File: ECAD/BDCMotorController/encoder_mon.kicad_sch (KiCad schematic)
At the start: 12 parts, among them U70 74AHC00, U71 74AHC00, U72 74AHC1G17, U73 74AHC1G17, U74 74AHC00

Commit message: Progressed ECAD.
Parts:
- renumbered C145 to C144, C146 to C145, C147 to C146, C148 to C147, C149 to C148, U70 to U69, U71 to U70, U72 to U71, U73 to U72, U74 to U73

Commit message: Progressed ECAD.
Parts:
- C144, C145, C148: Status OK -> (none)
- R68, R69: MPN AC0805FR-7W1KL -> (none)
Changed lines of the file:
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@@
 			)
 		)
-		(property "Status" "OK"
+		(property "Status" ""
 			(at 135.89 173.99 0)
 			(effects
@@
 			)
 		)
-		(property "Status" "OK"
+		(property "Status" ""
 			(at 83.82 172.72 0)
 			(effects
@@
 			)
 		)
-		(property "Datasheet" "https://datasheet.lcsc.com/lcsc/2010202005_YAGEO-AC0805FR-7W1KL_C727989.pdf"
+		(property "Datasheet" ""
 			(at 92.71 111.76 0)
 			(effects
@@
 			)
 		)
-		(property "MPN" "AC0805FR-7W1KL"
+		(property "MPN" ""
 			(at 92.71 111.76 90)
 			(effects
@@
 			)
 		)
-		(property "Datasheet" "https://datasheet.lcsc.com/lcsc/2010202005_YAGEO-AC0805FR-7W1KL_C727989.pdf"
+		(property "Datasheet" ""
 			(at 92.71 68.58 0)
 			(effects
@@
 			)
 		)
-		(property "MPN" "AC0805FR-7W1KL"
+		(property "MPN" ""
 			(at 92.71 68.58 90)
 			(effects
@@
 			)
 		)
-		(property "Status" "OK"
+		(property "Status" ""
 			(at 31.75 175.26 0)
 			(effects

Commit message: Progressed ECAD.
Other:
- note added: "333us min"
- note added: "Input square wave max frequency = 3 kHz (typical hall efect encoder frequency at max motor speed with no load)"
- note added: "t"
- note added: "tmin = 62.5ns @ fMCU = 16MHz"
- moved on the sheet: C146, C147, R68, R69, U69A, U69B, U69C, U69D, U70A, U70B, U70C, U70D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

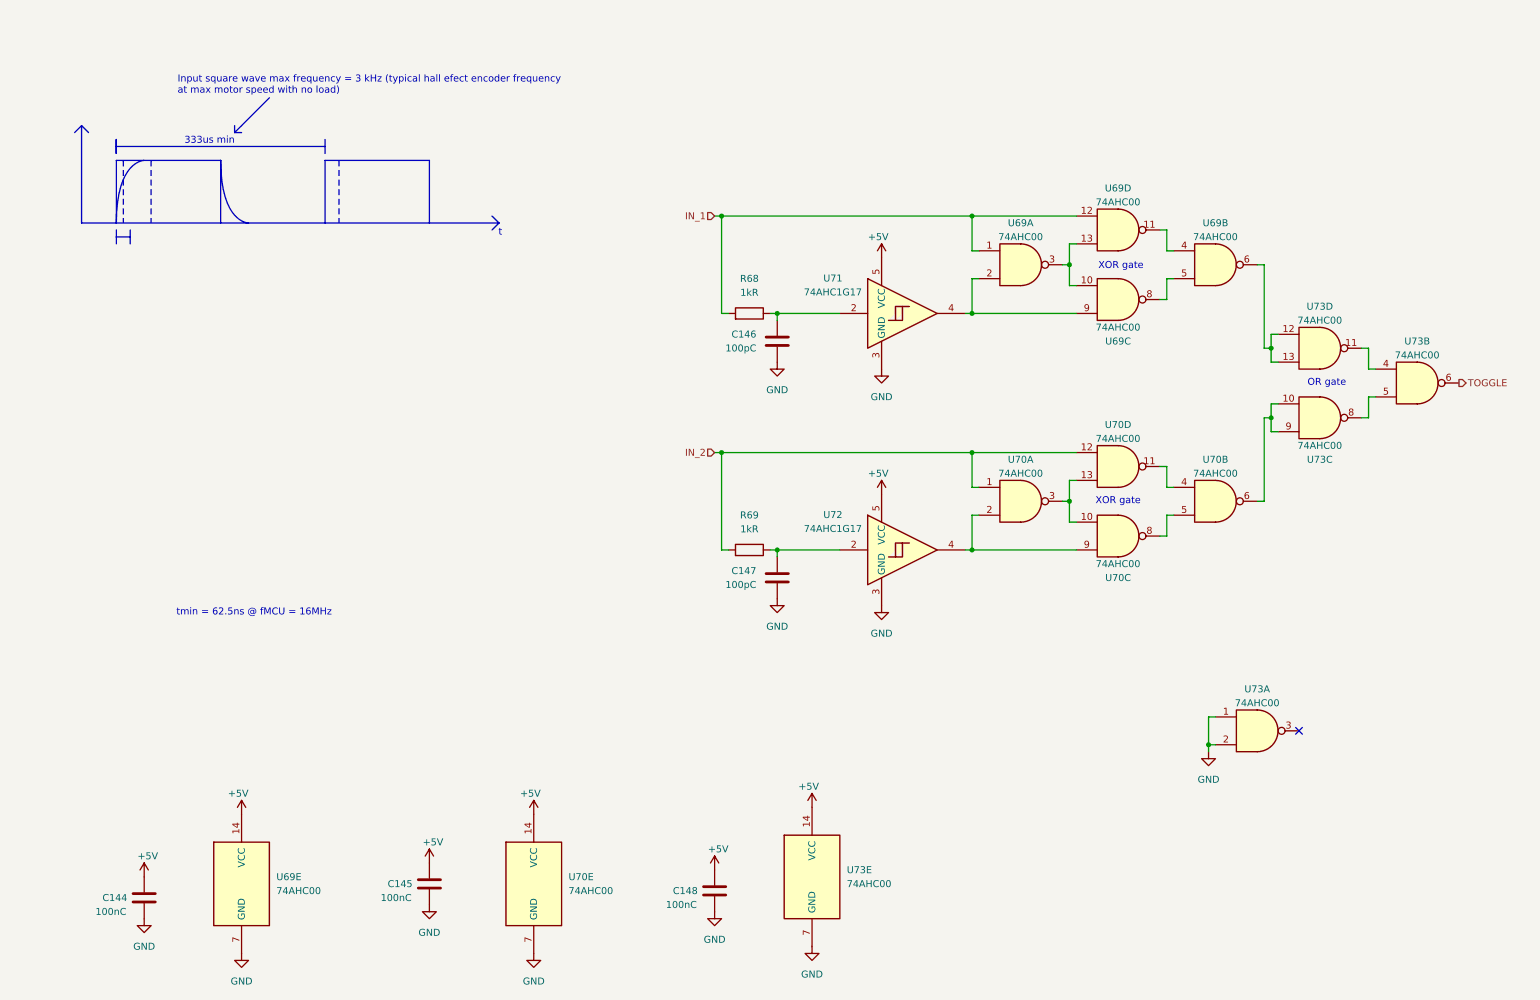
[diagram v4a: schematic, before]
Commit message: Update encoder_mon.kicad_sch
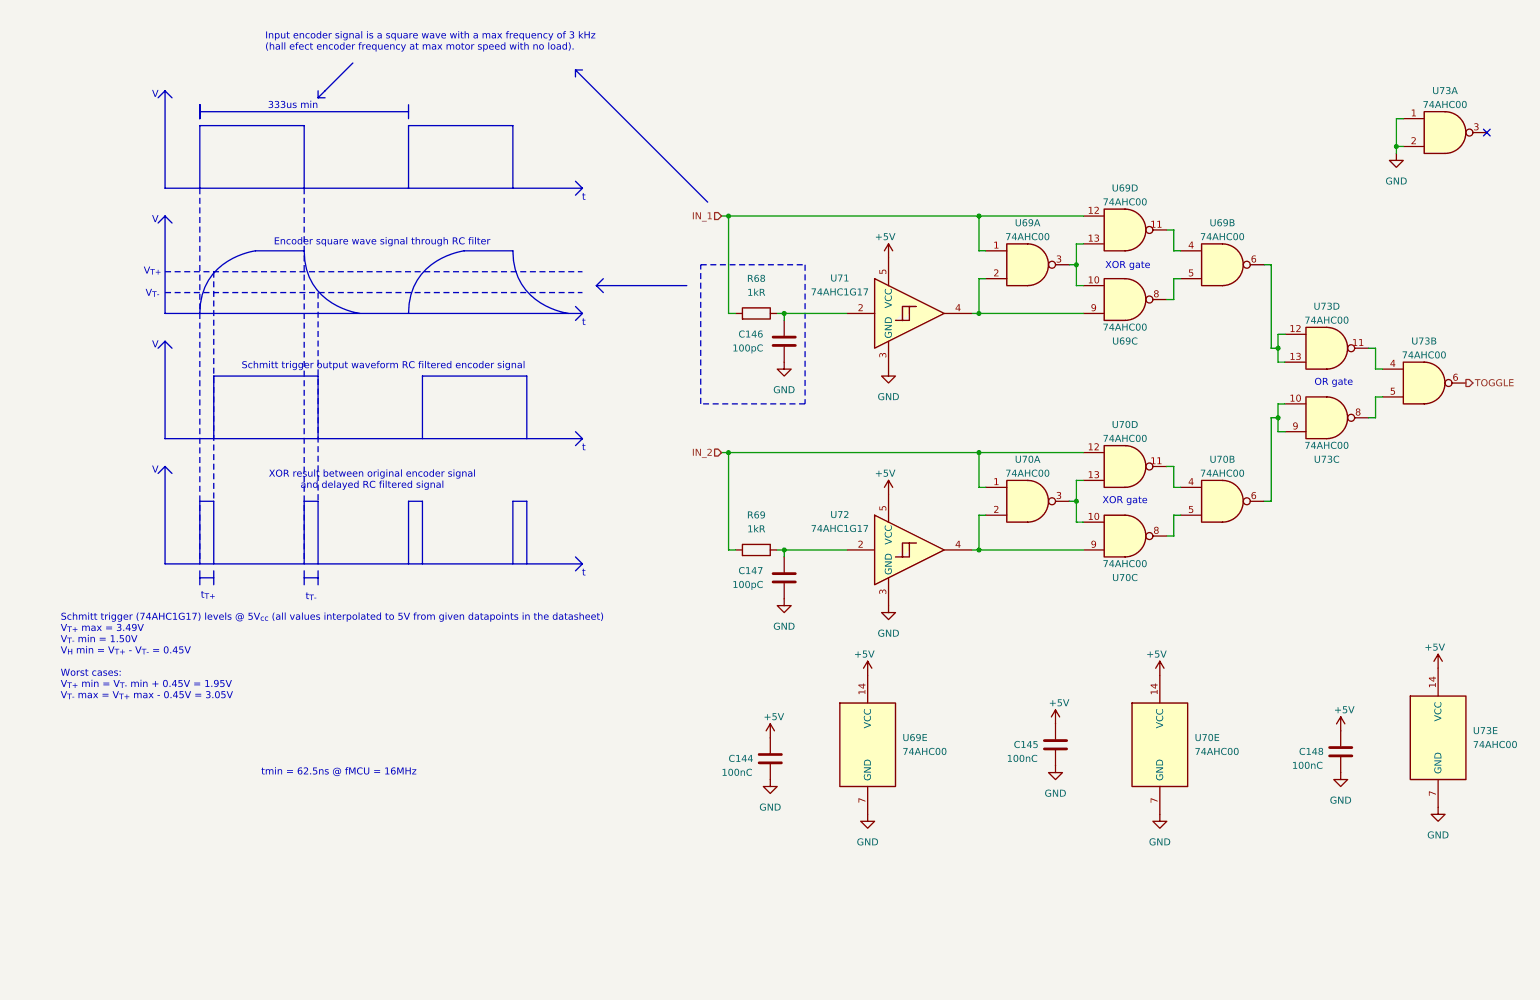
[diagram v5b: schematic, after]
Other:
- note added: "Encoder square wave signal through RC filter"
- note added: "Input encoder signal is a square wave with a max frequency of 3 kHz (hall efect encoder frequency at max motor speed with no load)."
- note added: "Schmitt trigger (74AHC1G17) levels @ 5V_{cc} (all values interpolated to 5V from given datapoints in the datasheet) V_{T+} max = 3.49V V_{T-} min = 1.50V V_{H} min = V_{T+} - V_{T-} = 0.45V Worst cases: V_{T+} min = V_{T-} min + 0.45V = 1.95V V_{T-} max = V_{T+} max - 0.45V = 3.05V"
- note added: "Schmitt trigger output waveform RC filtered encoder signal"
- note added: "V"
- note added: "V_{T+}"
- note added: "V_{T-}"
- note added: "XOR result between original encoder signal and delayed RC filtered signal"
- note added: "t_{T+}"
- note added: "t_{T-}"
- note removed: "Input square wave max frequency = 3 kHz (typical hall efect encoder frequency at max motor speed with no load)"
- moved on the sheet: C144, C145, C146, C147, C148, R68, R69, U69A, U69B, U69C, U69D, U69E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

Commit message: Progressed ECAD.
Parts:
- removed C147: 100pC, Capacitor_SMD:C_0805_2012Metric, symbol Device:C
- added C164: 100nC, Capacitor_SMD:C_0805_2012Metric, symbol Device:C
- C146: value 100pC -> 100nC; MPN CC0805KRX7R9BB101 -> (none); Status OK -> (none)
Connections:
- net GND: now also C164.2
- net at R68.1, U71.2: now also C164.1; no longer C146.1
- net at R69.1, U72.2: now also C146.1
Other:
- note added: "62.5ns < t_{T+} < 333us / 2 62.5ns < RC charging to V_{T+} min and V_{T+} max < 166.5us RC charging time to 99.9% < 166.5us"
- note added: "62.5ns < t_{T+} < 333us / 2 62.5ns < RC discharging to V_{T-} min and V_{T-} max < 166.5us"
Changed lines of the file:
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@@
 		)
 	)
+	(text "62.5ns < t_{T+} < 333us / 2\n62.5ns < RC discharging to V_{T-} min and V_{T-} max < 166.5us"
+		(exclude_from_sim no)
+		(at 46.736 176.784 0)
+		(effects
+			(font
+				(size 1.27 1.27)
+			)
+		)
+	)
 	(text "V"
 		(exclude_from_sim no)
@@
 		)
 	)
+	(text "62.5ns < t_{T+} < 333us / 2\n62.5ns < RC charging to V_{T+} min and V_{T+} max < 166.5us\n\nRC charging time to 99.9% < 166.5us"
+		(exclude_from_sim no)
+		(at 44.704 160.528 0)
+		(effects
+			(font
+				(size 1.27 1.27)
+			)
+		)
+	)
 	(text "V"
 		(exclude_from_sim no)
@@
 	)
 	(symbol
+		(lib_id "Device:C")
+		(at 148.59 73.66 0)
+		(unit 1)
+		(exclude_from_sim no)
+		(in_bom yes)
+		(on_board yes)
+		(dnp no)
+		(property "Reference" "C164"
+			(at 140.97 73.66 0)
+			(effects
+				(font
+					(size 1.27 1.27)
+				)
+				(justify left)
+			)
+		)
+		(property "Value" "100nC"
+			(at 139.7 76.2 0)
+			(effects
+				(font
+					(size 1.27 1.27)
+				)
+				(justify left)
+			)
+		)
+		(property "Footprint" "Capacitor_SMD:C_0805_2012Metric"
+			(at 149.5552 77.47 0)
+			(effects
+				(font
+					(size 1.27 1.27)
+				)
+				(hide yes)
+			)
+		)
+		(property "Datasheet" ""
+			(at 148.59 73.66 0)
+			(effects
+				(font
+					(size 1.27 1.27)
+				)
+				(hide yes)
+			)
+		)
+		(property "Description" ""
+			(at 148.59 73.66 0)
+			(effects
+				(font
+					(size 1.27 1.27)
+				)
+			)
+		)
+		(property "MPN" ""
+			(at 148.59 73.66 0)
+			(effects
+				(font
+					(size 1.27 1.27)
+				)
+				(hide yes)
+			)
+		)
+		(property "Status" ""
+			(at 148.59 73.66 0)
+			(effects
+				(font
+					(size 1.27 1.27)
+				)
+				(hide yes)
+			)
+		)
+		(property "Sim.Device" ""
+			(at 148.59 73.66 0)
+			(effects
+				(font
+					(size 1.27 1.27)
+				)
+				(hide yes)
+			)
+		)
+		(property "Sim.Pins" ""
+			(at 148.59 73.66 0)
+			(effects
+				(font
+					(size 1.27 1.27)
+				)
+				(hide yes)
+			)
+		)
+		(pin "1"
+		)
+		(pin "2"
+		)
+		(instances
+			(project "BDCMotorController"
+				(path "/e63e39d7-6ac0-4ffd-8aa3-1841a4541b55/db5ef6f2-ef2e-48a9-8a35-f048f36a95fd/7332c390-df69-4887-9955-5042bba45ea6"
+					(reference "C165")
+					(unit 1)
+				)
+				(path "/e63e39d7-6ac0-4ffd-8aa3-1841a4541b55/db5ef6f2-ef2e-48a9-8a35-f048f36a95fd/900f150c-7ff8-4dd3-b80e-d3977fed4d00"
+					(reference "C164")
+					(unit 1)
+				)
+			)
+		)
+	)
+	(symbol
 		(lib_id "74xx:74HC00")
 		(at 228.6 59.69 0)
@@
 	(symbol
 		(lib_id "Device:C")
-		(at 148.59 73.66 0)
-		(mirror y)
+		(at 148.59 116.84 0)
 		(unit 1)
 		(exclude_from_sim no)
@@
 		(dnp no)
 		(property "Reference" "C146"
-			(at 144.78 72.3899 0)
+			(at 140.97 116.84 0)
 			(effects
 				(font
@@
 			)
 		)
-		(property "Value" "100pC"
-			(at 144.78 74.9299 0)
+		(property "Value" "100nC"
+			(at 139.7 119.38 0)
 			(effects
 				(font
@@
 		)
 		(property "Footprint" "Capacitor_SMD:C_0805_2012Metric"
-			(at 147.6248 77.47 0)
+			(at 149.5552 120.65 0)
 			(effects
 				(font
@@
 			)
 		)
-		(property "Datasheet" "https://lcsc.com/datasheet/lcsc_datasheet_2506131735_YAGEO-CC0805KRX7R9BB101_C107140.pdf"
-			(at 148.59 73.66 0)
+		(property "Datasheet" ""
+			(at 148.59 116.84 0)
 			(effects
 				(font
@@
 			)
 		)
-		(property "Description" "Unpolarized capacitor"
-			(at 148.59 73.66 0)
+		(property "Description" ""
+			(at 148.59 116.84 0)
 			(effects
 				(font
 					(size 1.27 1.27)
 				)
-				(hide yes)
 			)
 		)
-		(property "MPN" "CC0805KRX7R9BB101"
-			(at 148.59 73.66 0)
+		(property "MPN" ""
+			(at 148.59 116.84 0)
 			(effects
 				(font
@@
 			)
 		)
-		(property "Status" "OK"
-			(at 148.59 73.66 0)
+		(property "Status" ""
+			(at 148.59 116.84 0)
 			(effects
 				(font
@@
 		)
 		(property "Sim.Device" ""
-			(at 148.59 73.66 0)
+			(at 148.59 116.84 0)
 			(effects
 				(font
@@
 		)
 		(property "Sim.Pins" ""
-			(at 148.59 73.66 0)
+			(at 148.59 116.84 0)
 			(effects
 				(font
@@
 			)
 		)
-		(pin "2"
-		)
 		(pin "1"
 		)
+		(pin "2"
+		)
 		(instances
 			(project "BDCMotorController"
 				(path "/e63e39d7-6ac0-4ffd-8aa3-1841a4541b55/db5ef6f2-ef2e-48a9-8a35-f048f36a95fd/7332c390-df69-4887-9955-5042bba45ea6"
-					(reference "C164")
+					(reference "C147")
 					(unit 1)
 				)
@@
 					(unit 1)
 				)
-			)
-		)
-	)
-	(symbol
-		(lib_id "Device:C")
-		(at 148.59 116.84 0)
-		(mirror y)
-		(unit 1)
-		(exclude_from_sim no)
-		(in_bom yes)
-		(on_board yes)
-		(dnp no)
-		(property "Reference" "C147"
-			(at 144.78 115.5699 0)
-			(effects
-				(font
-					(size 1.27 1.27)
-				)
-				(justify left)
-			)
-		)
-		(property "Value" "100pC"
-			(at 144.78 118.1099 0)
-			(effects
-				(font
-					(size 1.27 1.27)
-				)
-				(justify left)
-			)
-		)
-		(property "Footprint" "Capacitor_SMD:C_0805_2012Metric"
-			(at 147.6248 120.65 0)
-			(effects
-				(font
-					(size 1.27 1.27)
-				)
-				(hide yes)
-			)
-		)
-		(property "Datasheet" "https://lcsc.com/datasheet/lcsc_datasheet_2506131735_YAGEO-CC0805KRX7R9BB101_C107140.pdf"
-			(at 148.59 116.84 0)
-			(effects
-				(font
-					(size 1.27 1.27)
-				)
-				(hide yes)
-			)
-		)
-		(property "Description" "Unpolarized capacitor"
-			(at 148.59 116.84 0)
-			(effects
-				(font
-					(size 1.27 1.27)
-				)
-				(hide yes)
-			)
-		)
-		(property "MPN" "CC0805KRX7R9BB101"
-			(at 148.59 116.84 0)
-			(effects
-				(font
-					(size 1.27 1.27)
-				)
-				(hide yes)
-			)
-		)
-		(property "Status" "OK"
-			(at 148.59 116.84 0)
-			(effects
-				(font
-					(size 1.27 1.27)
-				)
-				(hide yes)
-			)
-		)
-		(property "Sim.Device" ""
-			(at 148.59 116.84 0)
-			(effects
-				(font
-					(size 1.27 1.27)
-				)
-				(hide yes)
-			)
-		)
-		(property "Sim.Pins" ""
-			(at 148.59 116.84 0)
-			(effects
-				(font
-					(size 1.27 1.27)
-				)
-				(hide yes)
-			)
-		)
-		(pin "2"
-		)
-		(pin "1"
-		)
-		(instances
-			(project "BDCMotorController"
-				(path "/e63e39d7-6ac0-4ffd-8aa3-1841a4541b55/db5ef6f2-ef2e-48a9-8a35-f048f36a95fd/7332c390-df69-4887-9955-5042bba45ea6"
-					(reference "C165")
-					(unit 1)
-				)
-				(path "/e63e39d7-6ac0-4ffd-8aa3-1841a4541b55/db5ef6f2-ef2e-48a9-8a35-f048f36a95fd/900f150c-7ff8-4dd3-b80e-d3977fed4d00"
-					(reference "C147")
-					(unit 1)
-				)

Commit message: Progressed ECAD.
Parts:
- removed C164: 100nC, Capacitor_SMD:C_0805_2012Metric, symbol Device:C
- added C145: 100pC, Capacitor_SMD:C_0805_2012Metric, symbol Device:C
- C146: value 100nC -> 100pC; MPN (none) -> CC0805KRX7R9BB101; Status (none) -> OK
- R68, R69: value 1kR -> 100kR; MPN (none) -> RT0805BRD07100KL
- renumbered C145 to C147, U71 to U70, U72 to U71, U70 to U72
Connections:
- net GND: now also C145.2
- net IN_1: now also R68.1; no longer R68.2
- net IN_2: now also R69.1; no longer R69.2
- net at U70.2: now also R68.2, C145.1; no longer R68.1
- net at C146.1, U71.2: now also R69.2; no longer R69.1
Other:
- note added: "1.50V < V_{T-} < 3.05V"
- note added: "1.95V < V_{T+} < 3.49V"
- note added: "167us min"
- note added: "4.4us < t_{T+} < 13.3us"
- note added: "4.4us < t_{T-} < 13.4us"
- note removed: "62.5ns < t_{T+} < 333us / 2 62.5ns < RC charging to V_{T+} min and V_{T+} max < 166.5us RC charging time to 99.9% < 166.5us"
- note removed: "62.5ns < t_{T+} < 333us / 2 62.5ns < RC discharging to V_{T-} min and V_{T-} max < 166.5us"
- note removed: "Schmitt trigger (74AHC1G17) levels @ 5V_{cc} (all values interpolated to 5V from given datapoints in the datasheet) V_{T+} max = 3.49V V_{T-} min = 1.50V V_{H} min = V_{T+} - V_{T-} = 0.45V Worst cases: V_{T+} min = V_{T-} min + 0.45V = 1.95V V_{T-} max = V_{T+} max - 0.45V = 3.05V"
- note removed: "V_{T+}"
- note removed: "V_{T-}"
- note removed: "t_{T+}"
- note removed: "t_{T-}"

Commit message: Progressed ECAD.
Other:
- note added: "Calculated from 74AHC1G17 datasheet"
- note added: "Given: - Input encoder maximum frequency - Schmitt trigger (74AHC1G17) parameters - usage of XOR logic gate to generate a pulse for each encoder signal transition an RC filter was chosen such as to produce enough delay to generate a pulse of enough duration for each encoder signal transition as to be detected by the MCU interrupt logic: t_{T+} and t_{T-} > tmin Also, the RC constant tau was chose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"
- note added: "Positive going transitions (T+) time intervals calculated from lowest V_{T+}. Negative going transitions (T-) time intervals calculated from highest V_{T-}."
- note added: "RC filter R = 100kohm +/- 1% C = 100pF +/- 10% tau = 10us +/- 1.1us"
- moved on the sheet: C144, C145, C146, C147, C148, R68, R69, U69A, U69B, U69C, U69D, U69E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
